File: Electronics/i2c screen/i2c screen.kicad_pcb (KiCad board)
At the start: 2 copper layers, 65 x 29 mm, 9 parts, among them J1 renc_con, J2 display_con, J3 display_in, SW1 Encoder

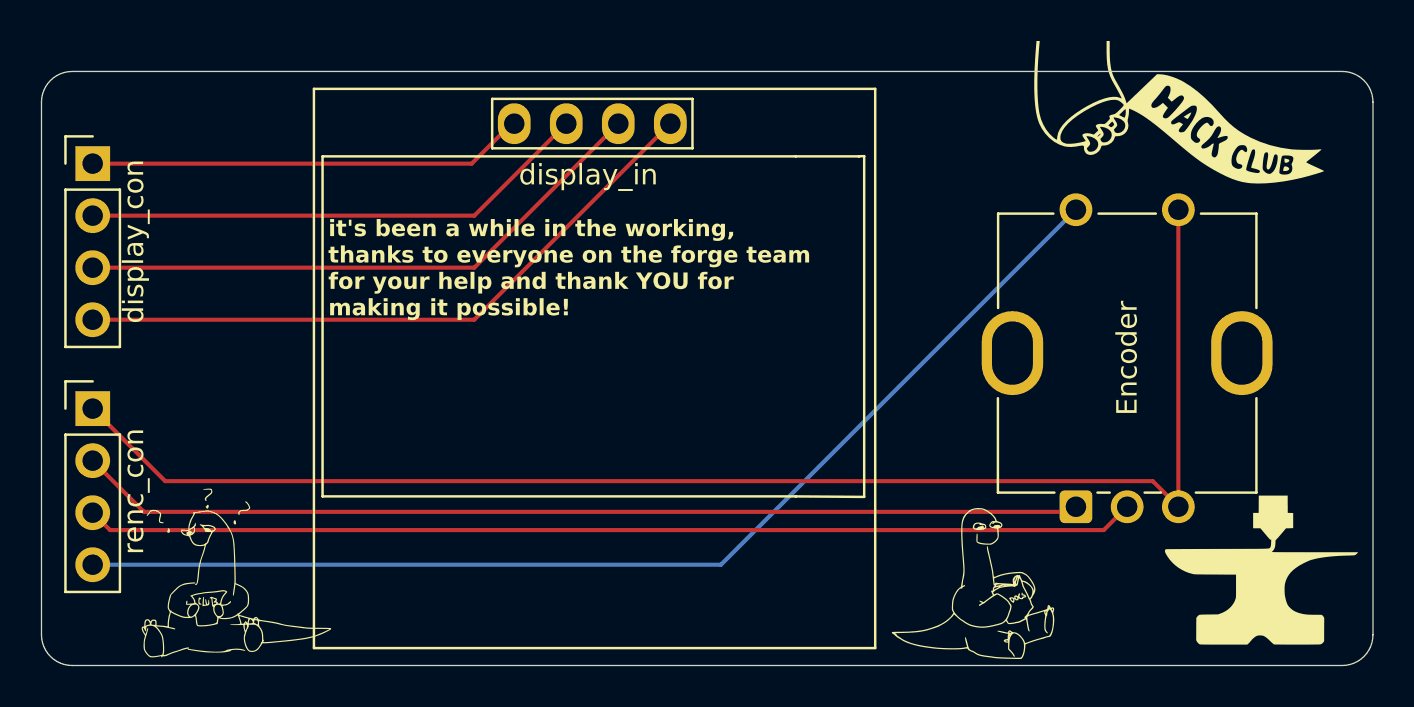
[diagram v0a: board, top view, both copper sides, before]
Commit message: mounting holes
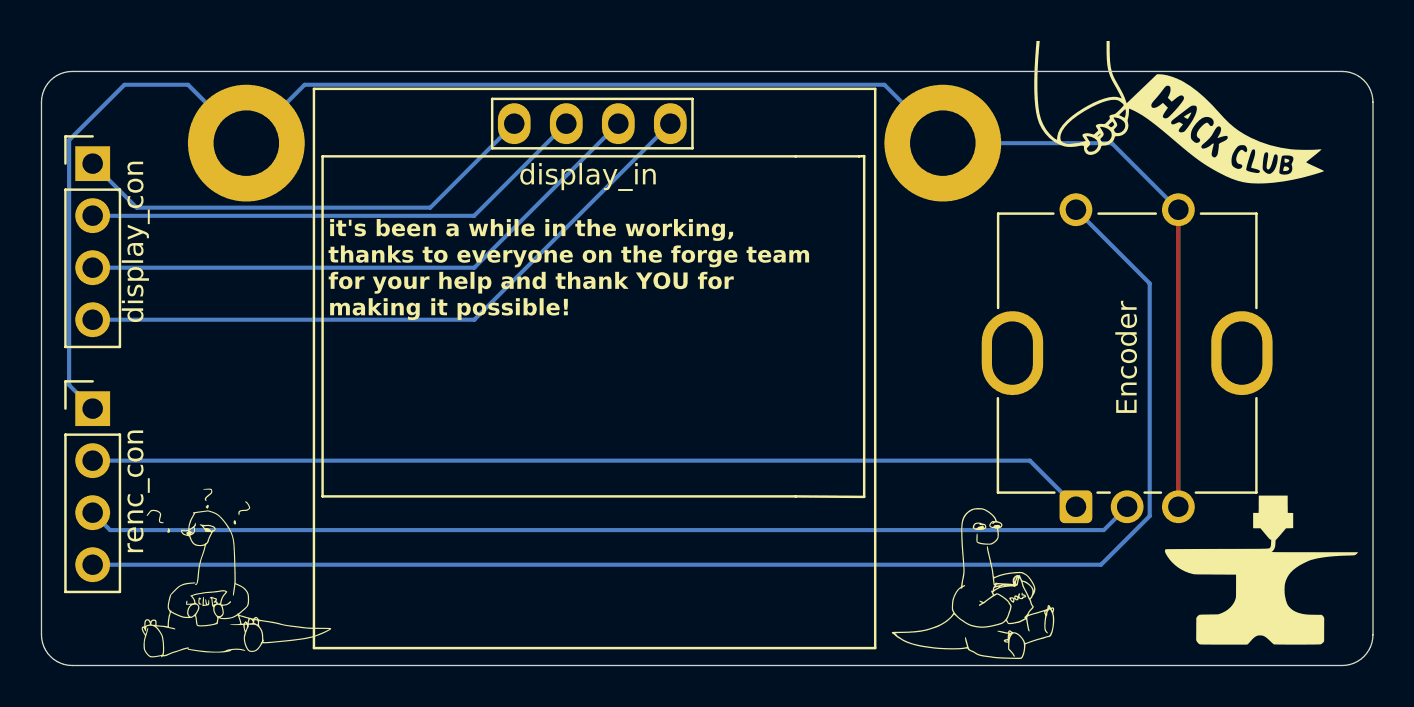
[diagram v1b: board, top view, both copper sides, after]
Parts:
- added H1: MountingHole_3.2mm_M3_ISO7380_Pad, MountingHole:MountingHole_3.2mm_M3_ISO7380_Pad, F.Cu at (140.0, 118.0)
- added H2: MountingHole_3.2mm_M3_ISO7380_Pad, MountingHole:MountingHole_3.2mm_M3_ISO7380_Pad, F.Cu at (174.0, 118.0)
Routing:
- net GNDREF: track 69.5 -> 88.2 mm
- net EN_BTN: track 55.2 -> 69.0 mm
- net Net-(J2-gnd): track 21.4 -> 23.2 mm
